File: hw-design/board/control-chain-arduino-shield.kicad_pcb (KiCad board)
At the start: 2 copper layers, 68.6 x 53.3 mm, 47 parts, among them J1 CC_INPUT, J2 CC_OUTPUT, P1 Power, P10 Power, P11 Analog, P12 Digital, P13 Digital, P2 Analog, P3 Digital, P4 Digital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

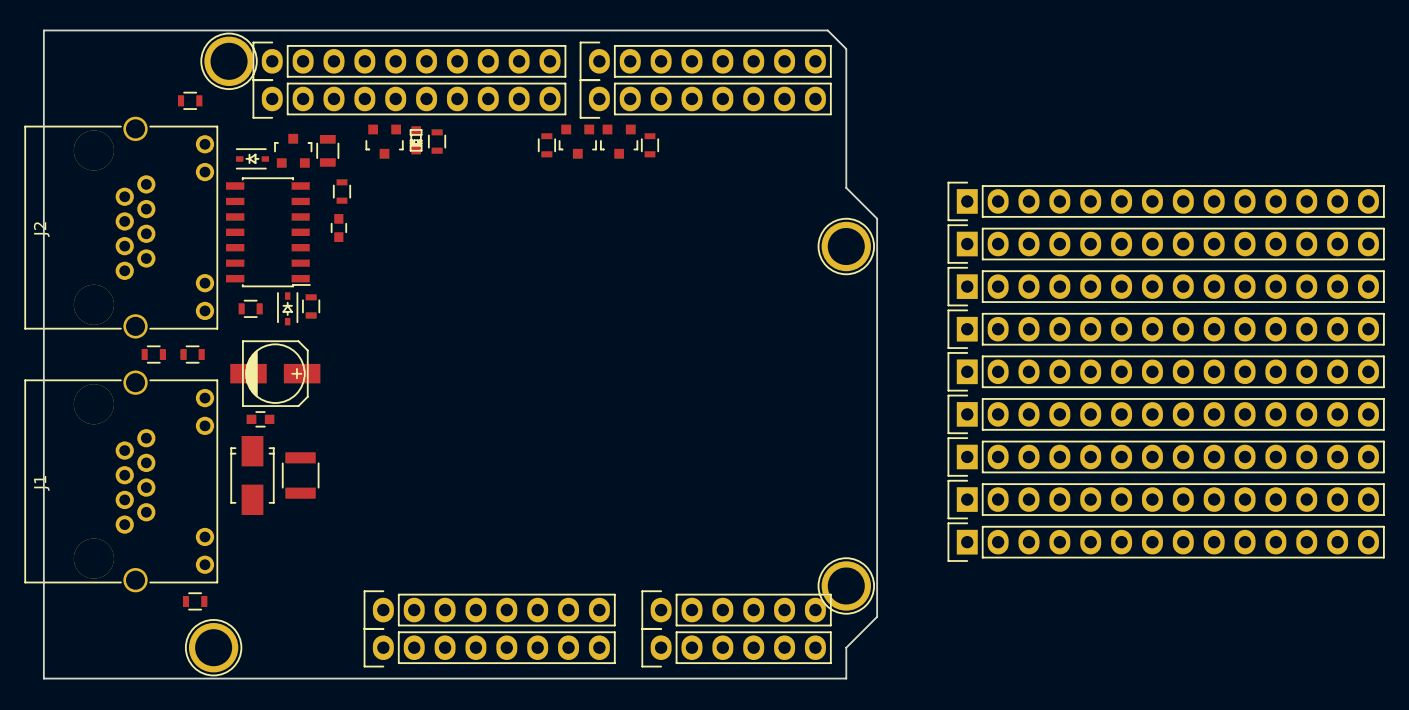
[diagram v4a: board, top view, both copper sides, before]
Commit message: pcb: design almost done, missing 2 or 3 tracks
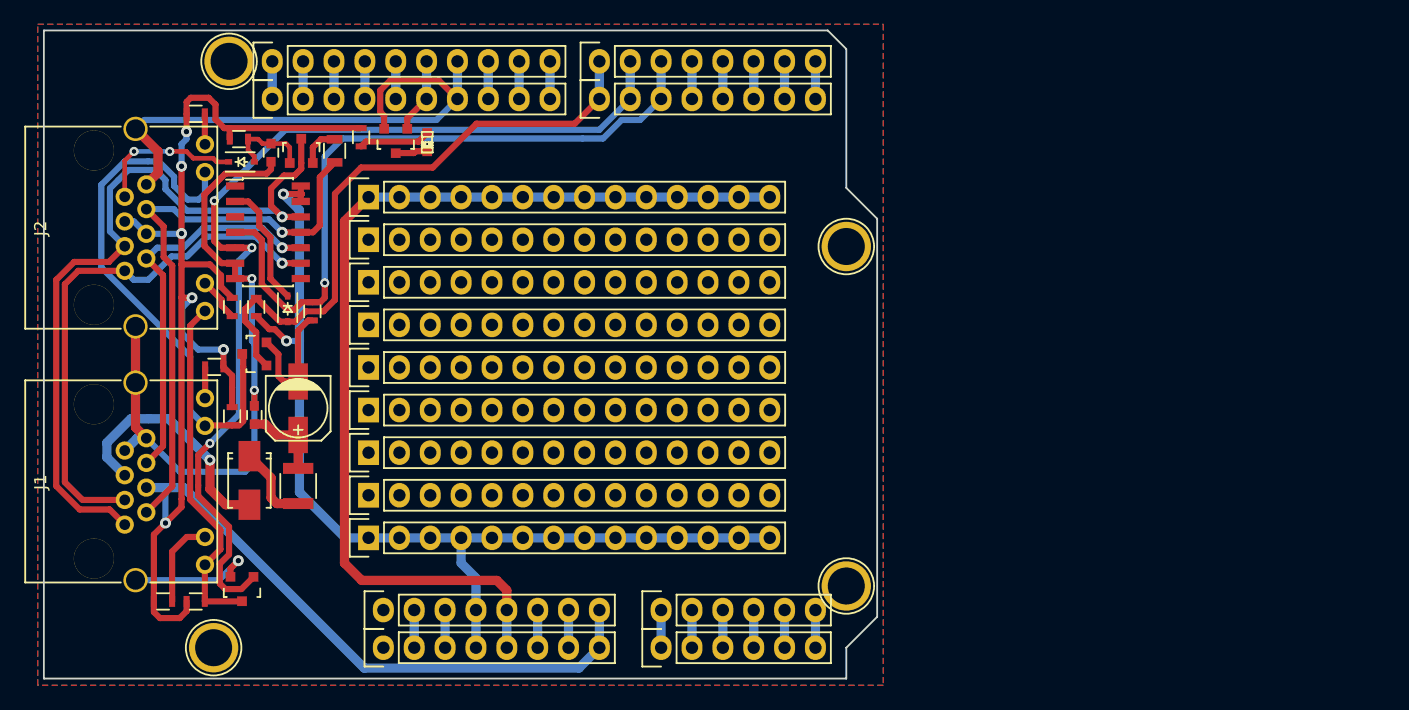
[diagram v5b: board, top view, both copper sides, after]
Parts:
- moved R7 53.0 mm to (123.5, 120.0), turned to 180 degrees
- moved P14 49.3 mm to (137.7, 97.3)
- moved P15 49.3 mm to (137.7, 93.8)
- moved P16 49.3 mm to (137.7, 90.2)
- moved P17 49.3 mm to (137.7, 107.8)
- moved P18 49.3 mm to (137.7, 111.3)
- moved P19 49.3 mm to (137.7, 114.8)
- moved P20 49.3 mm to (137.7, 86.7)
- moved P21 49.3 mm to (137.7, 100.8)
- moved P9 49.3 mm to (137.7, 104.3)
- moved Q3 48.2 mm to (127.3, 119.0)
- moved R6 34.2 mm to (126.5, 104.8)
- moved Q2 31.8 mm to (128.3, 99.6), turned to 90 degrees
- moved R8 9.52 mm to (127.1, 82.0), turned to 0 degrees
- moved C3 8.34 mm to (129.7, 83.1)
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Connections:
- J1 pad : (no net) -> GNDD
- J2 pad : (no net) -> GNDD
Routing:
- net +9V: track 0.00 -> 138.5 mm, vias 0 -> 6
- net GNDD: track 0.00 -> 131.2 mm, vias 0 -> 3
- net +5V: track 0.00 -> 83.0 mm
- net +3V3: track 0.00 -> 82.3 mm, vias 0 -> 2
- net IO1/TXD: track 0.00 -> 81.7 mm, vias 0 -> 3
- net RS485_RX+: track 0.00 -> 62.7 mm, vias 0 -> 1
- net IO2: track 0.00 -> 57.0 mm, vias 0 -> 1
- net IO0/RXD: track 0.00 -> 51.5 mm
- net RS485_RX-: track 0.00 -> 47.7 mm, vias 0 -> 1
- net RS485_RX_LED: track 0.00 -> 45.3 mm
- net RS485_TX+: track 0.00 -> 44.4 mm, vias 0 -> 1
- net RS485_TX-: track 0.00 -> 32.4 mm, vias 0 -> 1
- net RS485_TX_LED: track 0.00 -> 29.0 mm
- net POWER_INPUT: track 0.00 -> 20.2 mm, vias 0 -> 1
- net Net-(D3-Pad1): track 0.00 -> 12.2 mm, vias 0 -> 2
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- added copper zone on B.Cu, net GNDD
- added copper zone on F.Cu, net GNDD

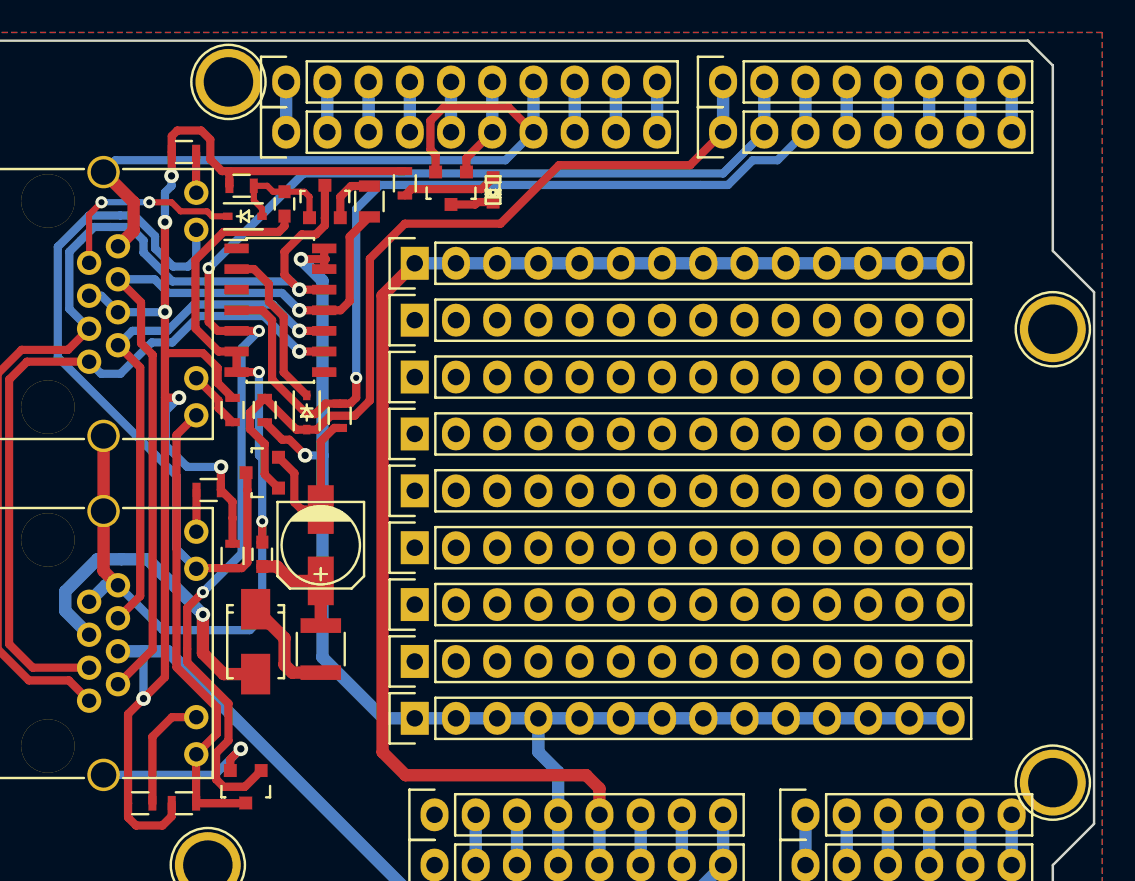
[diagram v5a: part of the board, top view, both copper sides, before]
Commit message: pcb: all tracks done + silkscreen of I/Os
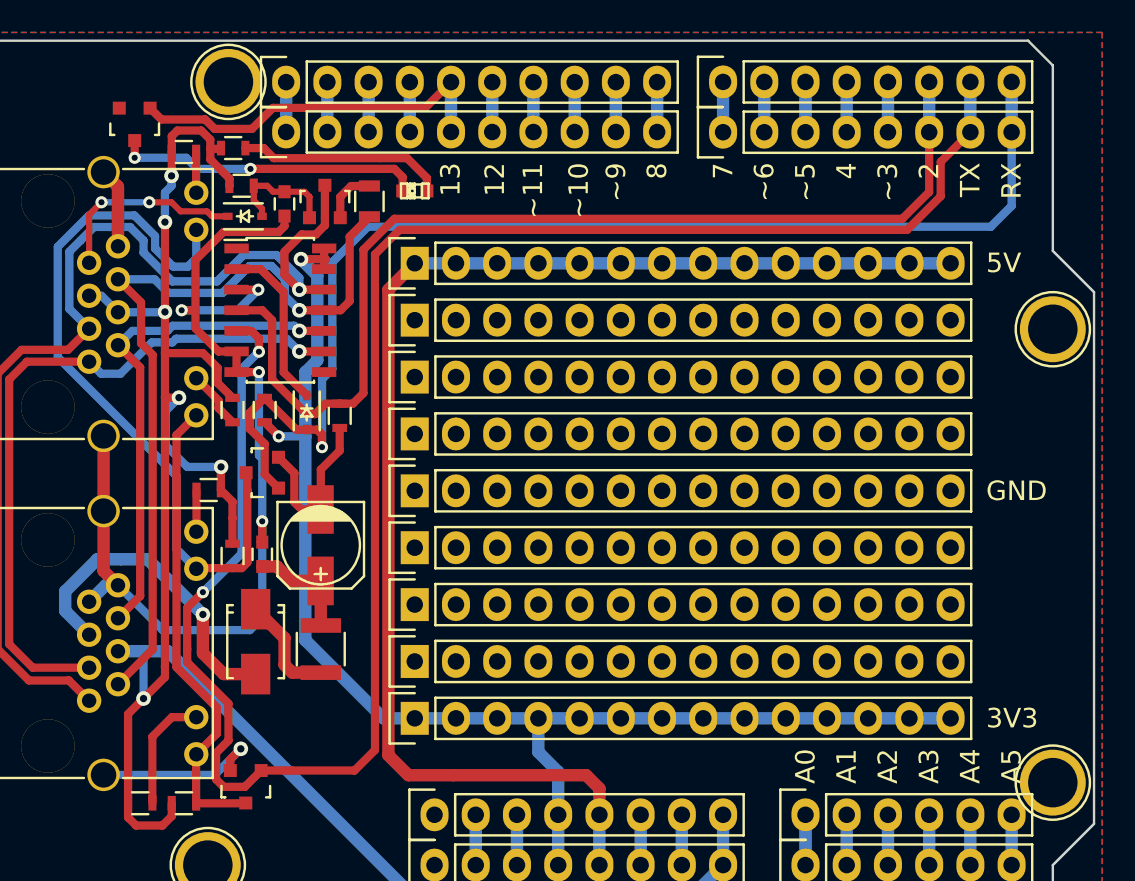
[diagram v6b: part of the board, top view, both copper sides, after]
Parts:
- moved Q1 19.9 mm to (120.5, 78.2)
- moved R1 10.8 mm to (126.5, 79.6), turned to 0 degrees
- moved D2 4.83 mm to (137.7, 82.3), turned to 0 degrees
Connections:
- P11 pad 1: AD5/SCL -> AD0
- P11 pad 2: AD4/SDA -> AD1
- P11 pad 3: AD3 -> AD2
- P11 pad 4: AD2 -> AD3
- P11 pad 5: AD1 -> AD4/SDA
- P11 pad 6: AD0 -> AD5/SCL
- P12 pad 1: IO8 -> AD5/SCL
- P12 pad 10: AD5/SCL -> IO8
- P12 pad 2: IO9 -> AD4/SDA
- P12 pad 3: IO10/SS -> AREF
- P12 pad 4: IO11/MOSI -> GNDD
- P12 pad 5: IO12/MISO -> IO13/SCK
- P12 pad 6: IO13/SCK -> IO12/MISO
- P12 pad 7: GNDD -> IO11/MOSI
- P12 pad 8: AREF -> IO10/SS
- P12 pad 9: AD4/SDA -> IO9
- P13 pad 1: IO0/RXD -> IO7
- P13 pad 2: IO1/TXD -> IO6
- P13 pad 3: IO2 -> IO5
- P13 pad 4: IO3 -> IO4
- P13 pad 5: IO4 -> IO3
- P13 pad 6: IO5 -> IO2
- P13 pad 7: IO6 -> IO1/TXD
- P13 pad 8: IO7 -> IO0/RXD
- P2 pad 1: AD5/SCL -> AD0
- P2 pad 2: AD4/SDA -> AD1
- P2 pad 3: AD3 -> AD2
- P2 pad 4: AD2 -> AD3
- P2 pad 5: AD1 -> AD4/SDA
- P2 pad 6: AD0 -> AD5/SCL
- P3 pad 1: IO8 -> AD5/SCL
- P3 pad 10: AD5/SCL -> IO8
- P3 pad 2: IO9 -> AD4/SDA
- P3 pad 3: IO10/SS -> AREF
- P3 pad 4: IO11/MOSI -> GNDD
- P3 pad 5: IO12/MISO -> IO13/SCK
- P3 pad 6: IO13/SCK -> IO12/MISO
- P3 pad 7: GNDD -> IO11/MOSI
- P3 pad 8: AREF -> IO10/SS
- P3 pad 9: AD4/SDA -> IO9
- P4 pad 1: IO0/RXD -> IO7
- P4 pad 2: IO1/TXD -> IO6
- P4 pad 3: IO2 -> IO5
- P4 pad 4: IO3 -> IO4
- P4 pad 5: IO4 -> IO3
- P4 pad 6: IO5 -> IO2
- P4 pad 7: IO6 -> IO1/TXD
- P4 pad 8: IO7 -> IO0/RXD
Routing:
- net IO1/TXD: track 81.7 -> 117.5 mm, vias 3 -> 2
- net GNDD: track 131.2 -> 99.6 mm, vias 3 -> 5
- net IO0/RXD: track 51.5 -> 74.5 mm, vias 0 -> 1
- net IO13/SCK: track 6.21 -> 23.4 mm
- net Net-(D2-Pad1): track 2.65 -> 18.9 mm, vias 0 -> 2
- net +9V: track 138.5 -> 128.1 mm
- net IO2: track 57.0 -> 65.1 mm, vias 1 -> 0
- net Net-(D2-Pad2): track 5.89 -> 12.8 mm
- net RS485_RX-: track 47.7 -> 49.7 mm
- net RS485_RX+: track 62.7 -> 64.5 mm
- net RS485_TX+: track 44.4 -> 43.2 mm
- net RS485_TX-: track 32.4 -> 31.3 mm
- net +3V3: track 82.3 -> 81.3 mm
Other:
- board text added: "12"
- board text added: "13"
- board text added: "2"
- board text added: "3V3"
- board text added: "4"
- board text added: "5V"
- board text added: "7"
- board text added: "8"
- board text added: "A0"
- board text added: "A1"
- board text added: "A2"
- board text added: "A3"
- board text added: "A4"
- board text added: "A5"
- board text added: "GND"
- board text added: "RX"
- board text added: "TX"
- board text added: "~~10"
- board text added: "~~11"
- board text added: "~~3"
- board text added: "~~5"
- board text added: "~~6"
- board text added: "~~9"
